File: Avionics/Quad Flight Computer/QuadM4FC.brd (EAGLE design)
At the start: 160 x 100 mm, 1 part, among them U1 INF-PG-LQFP-100-11-7000X7000E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

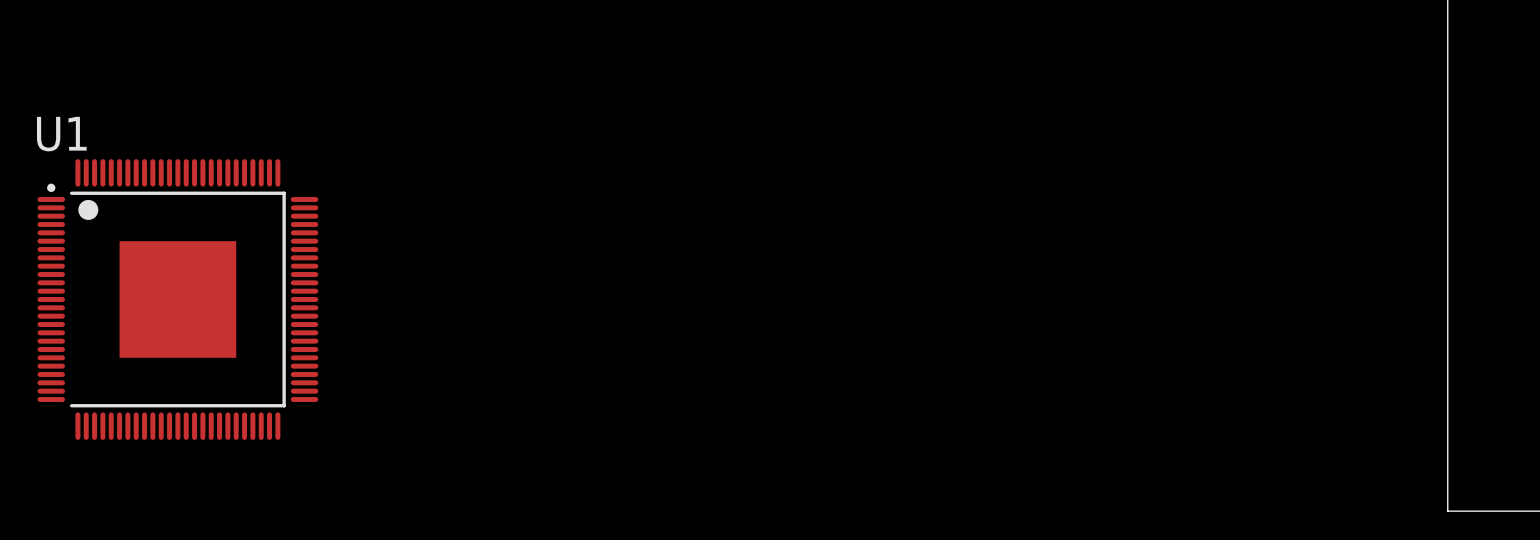
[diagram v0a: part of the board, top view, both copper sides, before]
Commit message: Added avionics library as Eagle-Library submodule.
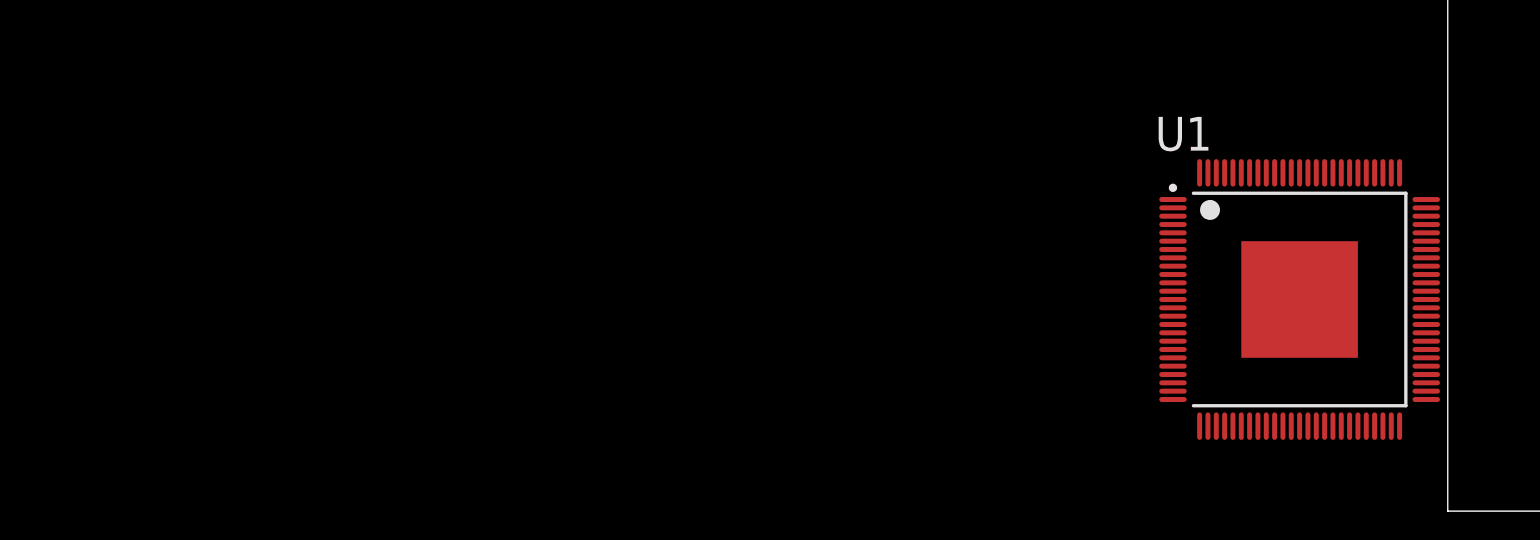
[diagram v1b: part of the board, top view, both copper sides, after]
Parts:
- moved U1 67.3 mm to (-8.89, 12.7)
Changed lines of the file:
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@@
 </autorouter>
 <elements>
-<element name="U1" library="XMC4500-F100K1024 AB" package="INF-PG-LQFP-100-11-7000X7000E9PRIMARY" value="INF-PG-LQFP-100-11-7000X7000E9LQFP-100" x="-76.2" y="12.7"/>
+<element name="U1" library="XMC4500-F100K1024 AB" package="INF-PG-LQFP-100-11-7000X7000E9PRIMARY" value="INF-PG-LQFP-100-11-7000X7000E9LQFP-100" x="-8.89" y="12.7"/>
 </elements>
 <signals>

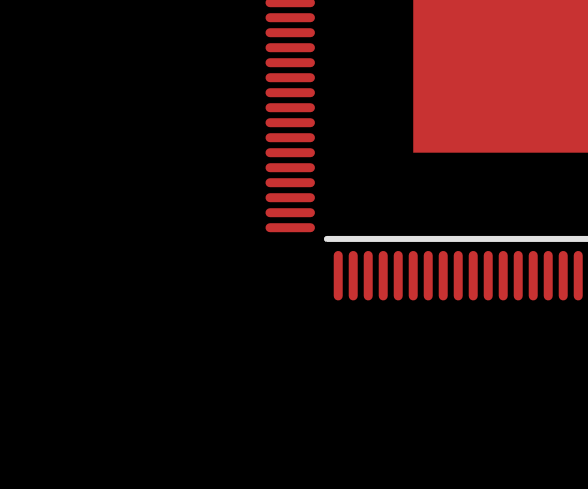
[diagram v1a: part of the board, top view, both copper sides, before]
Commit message: Added IMU to library
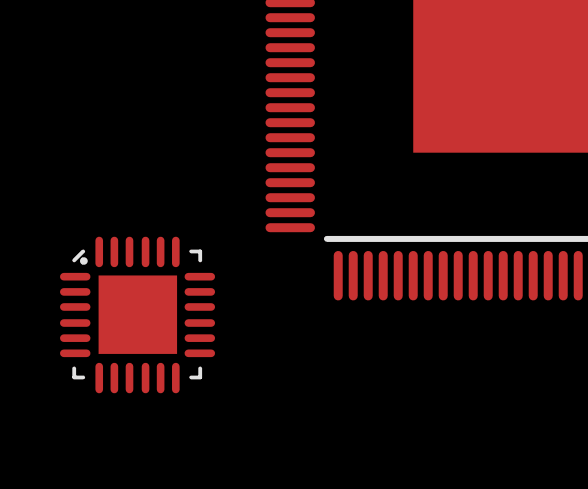
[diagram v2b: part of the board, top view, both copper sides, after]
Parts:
- added U2: MPU-9250, Invesense:QFN-24-4MM2
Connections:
- new net GND: U2.18, U2.P$1
- new net RESV_GND: U2.20
- new net RESV_VDDIO: U2.1
- new net VDD: U2.13
- new net VDDIO: U2.8
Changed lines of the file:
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@@
 <layer number="48" name="Document" color="7" fill="1" visible="yes" active="yes"/>
 <layer number="49" name="Reference" color="7" fill="1" visible="yes" active="yes"/>
+<layer number="50" name="dxf" color="7" fill="1" visible="yes" active="yes"/>
 <layer number="51" name="tDocu" color="7" fill="1" visible="yes" active="yes"/>
 <layer number="52" name="bDocu" color="7" fill="1" visible="yes" active="yes"/>
+<layer number="53" name="tGND_GNDA" color="7" fill="1" visible="yes" active="yes"/>
+<layer number="54" name="bGND_GNDA" color="7" fill="1" visible="yes" active="yes"/>
+<layer number="56" name="wert" color="7" fill="1" visible="yes" active="yes"/>
 <layer number="91" name="Nets" color="2" fill="1" visible="no" active="no"/>
 <layer number="92" name="Busses" color="1" fill="1" visible="no" active="no"/>
@@
 <layer number="97" name="Info" color="7" fill="1" visible="no" active="no"/>
 <layer number="98" name="Guide" color="6" fill="1" visible="no" active="no"/>
+<layer number="100" name="Muster" color="7" fill="1" visible="yes" active="yes"/>
+<layer number="101" name="Patch_Top" color="7" fill="1" visible="yes" active="yes"/>
+<layer number="102" name="Vscore" color="7" fill="1" visible="yes" active="yes"/>
+<layer number="103" name="tMap" color="7" fill="1" visible="yes" active="yes"/>
+<layer number="104" name="Name" color="7" fill="1" visible="yes" active="yes"/>
+<layer number="105" name="tPlate" color="7" fill="1" visible="yes" active="yes"/>
+<layer number="106" name="bPlate" color="7" fill="1" visible="yes" active="yes"/>
+<layer number="107" name="Crop" color="7" fill="1" visible="yes" active="yes"/>
+<layer number="108" name="fp8" color="7" fill="1" visible="yes" active="yes"/>
+<layer number="109" name="fp9" color="7" fill="1" visible="yes" active="yes"/>
+<layer number="110" name="fp0" color="7" fill="1" visible="yes" active="yes"/>
+<layer number="116" name="Patch_BOT" color="7" fill="1" visible="yes" active="yes"/>
+<layer number="121" name="_tsilk" color="7" fill="1" visible="yes" active="yes"/>
+<layer number="122" name="_bsilk" color="7" fill="1" visible="yes" active="yes"/>
+<layer number="123" name="tTestmark" color="7" fill="1" visible="yes" active="yes"/>
+<layer number="124" name="bTestmark" color="7" fill="1" visible="yes" active="yes"/>
+<layer number="125" name="_tNames" color="7" fill="1" visible="yes" active="yes"/>
+<layer number="131" name="tAdjust" color="7" fill="1" visible="yes" active="yes"/>
+<layer number="132" name="bAdjust" color="7" fill="1" visible="yes" active="yes"/>
+<layer number="144" name="Drill_legend" color="7" fill="1" visible="yes" active="yes"/>
+<layer number="151" name="HeatSink" color="7" fill="1" visible="yes" active="yes"/>
+<layer number="199" name="Contour" color="7" fill="1" visible="yes" active="yes"/>
+<layer number="200" name="200bmp" color="7" fill="1" visible="yes" active="yes"/>
+<layer number="201" name="201bmp" color="7" fill="1" visible="yes" active="yes"/>
+<layer number="202" name="202bmp" color="7" fill="1" visible="yes" active="yes"/>
+<layer number="203" name="203bmp" color="7" fill="1" visible="yes" active="yes"/>
+<layer number="204" name="204bmp" color="7" fill="1" visible="yes" active="yes"/>
+<layer number="205" name="205bmp" color="7" fill="1" visible="yes" active="yes"/>
+<layer number="206" name="206bmp" color="7" fill="1" visible="yes" active="yes"/>
+<layer number="207" name="207bmp" color="7" fill="1" visible="yes" active="yes"/>
+<layer number="208" name="208bmp" color="7" fill="1" visible="yes" active="yes"/>
+<layer number="209" name="209bmp" color="7" fill="1" visible="yes" active="yes"/>
+<layer number="210" name="210bmp" color="7" fill="1" visible="yes" active="yes"/>
+<layer number="211" name="211bmp" color="7" fill="1" visible="yes" active="yes"/>
+<layer number="212" name="212bmp" color="7" fill="1" visible="yes" active="yes"/>
+<layer number="213" name="213bmp" color="7" fill="1" visible="yes" active="yes"/>
+<layer number="214" name="214bmp" color="7" fill="1" visible="yes" active="yes"/>
+<layer number="215" name="215bmp" color="7" fill="1" visible="yes" active="yes"/>
+<layer number="216" name="216bmp" color="7" fill="1" visible="yes" active="yes"/>
+<layer number="217" name="217bmp" color="7" fill="1" visible="yes" active="yes"/>
+<layer number="218" name="218bmp" color="7" fill="1" visible="yes" active="yes"/>
+<layer number="219" name="219bmp" color="7" fill="1" visible="yes" active="yes"/>
+<layer number="220" name="220bmp" color="7" fill="1" visible="yes" active="yes"/>
+<layer number="221" name="221bmp" color="7" fill="1" visible="yes" active="yes"/>
+<layer number="222" name="222bmp" color="7" fill="1" visible="yes" active="yes"/>
+<layer number="223" name="223bmp" color="7" fill="1" visible="yes" active="yes"/>
+<layer number="224" name="224bmp" color="7" fill="1" visible="yes" active="yes"/>
+<layer number="250" name="Descript" color="7" fill="1" visible="yes" active="yes"/>
+<layer number="251" name="SMDround" color="7" fill="1" visible="yes" active="yes"/>
+<layer number="254" name="cooling" color="7" fill="1" visible="yes" active="yes"/>
 </layers>
 <board>
@@
 <elements>
 <element name="U1" library="XMC4500-F100K1024 AB" package="INF-PG-LQFP-100-11-7000X7000E9PRIMARY" value="INF-PG-LQFP-100-11-7000X7000E9LQFP-100" x="-8.89" y="12.7"/>
+<element name="U2" library="Invesense" package="QFN-24-4MM2" value="MPU-9250" x="-21.59" y="3.81"/>
 </elements>
 <signals>
+<signal name="GND">
+<contactref element="U2" pad="P$1"/>
+<contactref element="U2" pad="18"/>
+<wire x1="-19.5038" y1="5.0667" x2="-21.57" y2="3.8" width="0" layer="19" extent="1-1"/>
+</signal>
+<signal name="VDD">
+<contactref element="U2" pad="13"/>
+</signal>
+<signal name="RESV_GND">
+<contactref element="U2" pad="20"/>
+</signal>
+<signal name="VDDIO">
+<contactref element="U2" pad="8"/>
+</signal>
+<signal name="RESV_VDDIO">
+<contactref element="U2" pad="1"/>
+</signal>
 </signals>
 </board>

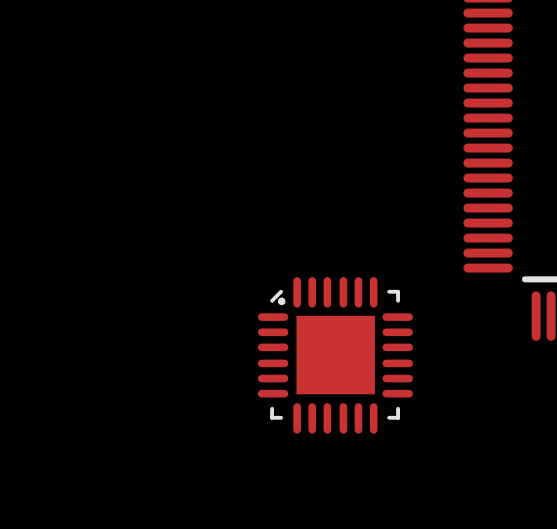
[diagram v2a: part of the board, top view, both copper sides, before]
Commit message: Added barometer
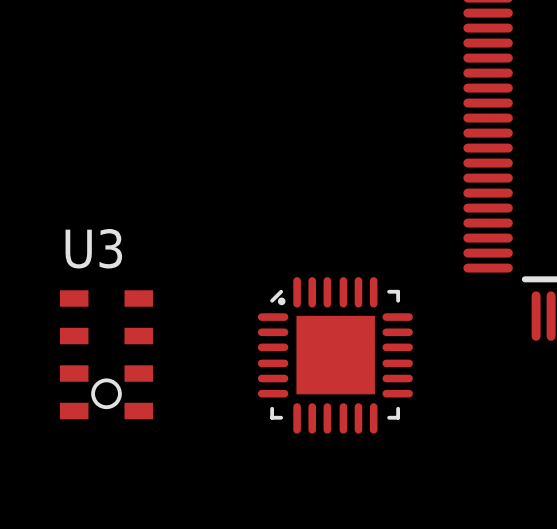
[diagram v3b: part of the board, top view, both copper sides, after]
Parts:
- added U3: MPL115A2, Sensors:MPL115A2
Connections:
- net GND: now also U2.EP; no longer U2.P$1
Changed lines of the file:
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@@
 <element name="U1" library="XMC4500-F100K1024 AB" package="INF-PG-LQFP-100-11-7000X7000E9PRIMARY" value="INF-PG-LQFP-100-11-7000X7000E9LQFP-100" x="-8.89" y="12.7"/>
 <element name="U2" library="Invesense" package="QFN-24-4MM2" value="MPU-9250" x="-21.59" y="3.81"/>
+<element name="U3" library="Sensors" package="MPL115A2" value="MPL115A2" x="-29.21" y="3.81"/>
 </elements>
 <signals>
 <signal name="GND">
-<contactref element="U2" pad="P$1"/>
 <contactref element="U2" pad="18"/>
+<contactref element="U2" pad="EP"/>
 <wire x1="-19.5038" y1="5.0667" x2="-21.57" y2="3.8" width="0" layer="19" extent="1-1"/>
 </signal>

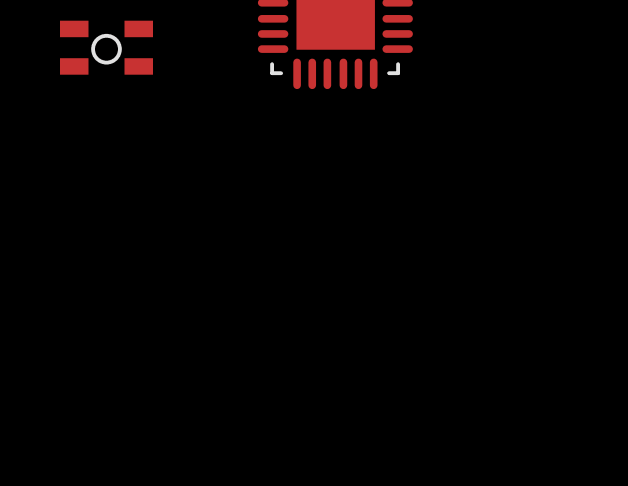
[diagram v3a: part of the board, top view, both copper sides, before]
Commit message: Added memory module
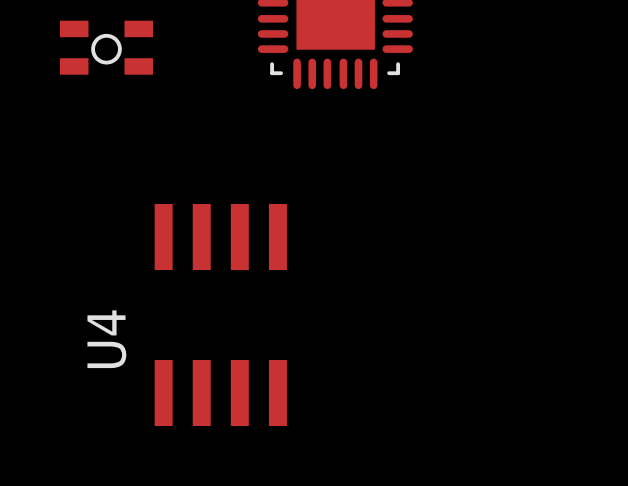
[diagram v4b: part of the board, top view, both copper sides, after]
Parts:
- added U4: S25FL127S, memory:SO8
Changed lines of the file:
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@@
 <element name="U2" library="Invesense" package="QFN-24-4MM2" value="MPU-9250" x="-21.59" y="3.81"/>
 <element name="U3" library="Sensors" package="MPL115A2" value="MPL115A2" x="-29.21" y="3.81"/>
+<element name="U4" library="memory" package="SO8" value="S25FL127S" x="-25.4" y="-6.35"/>
 </elements>
 <signals>

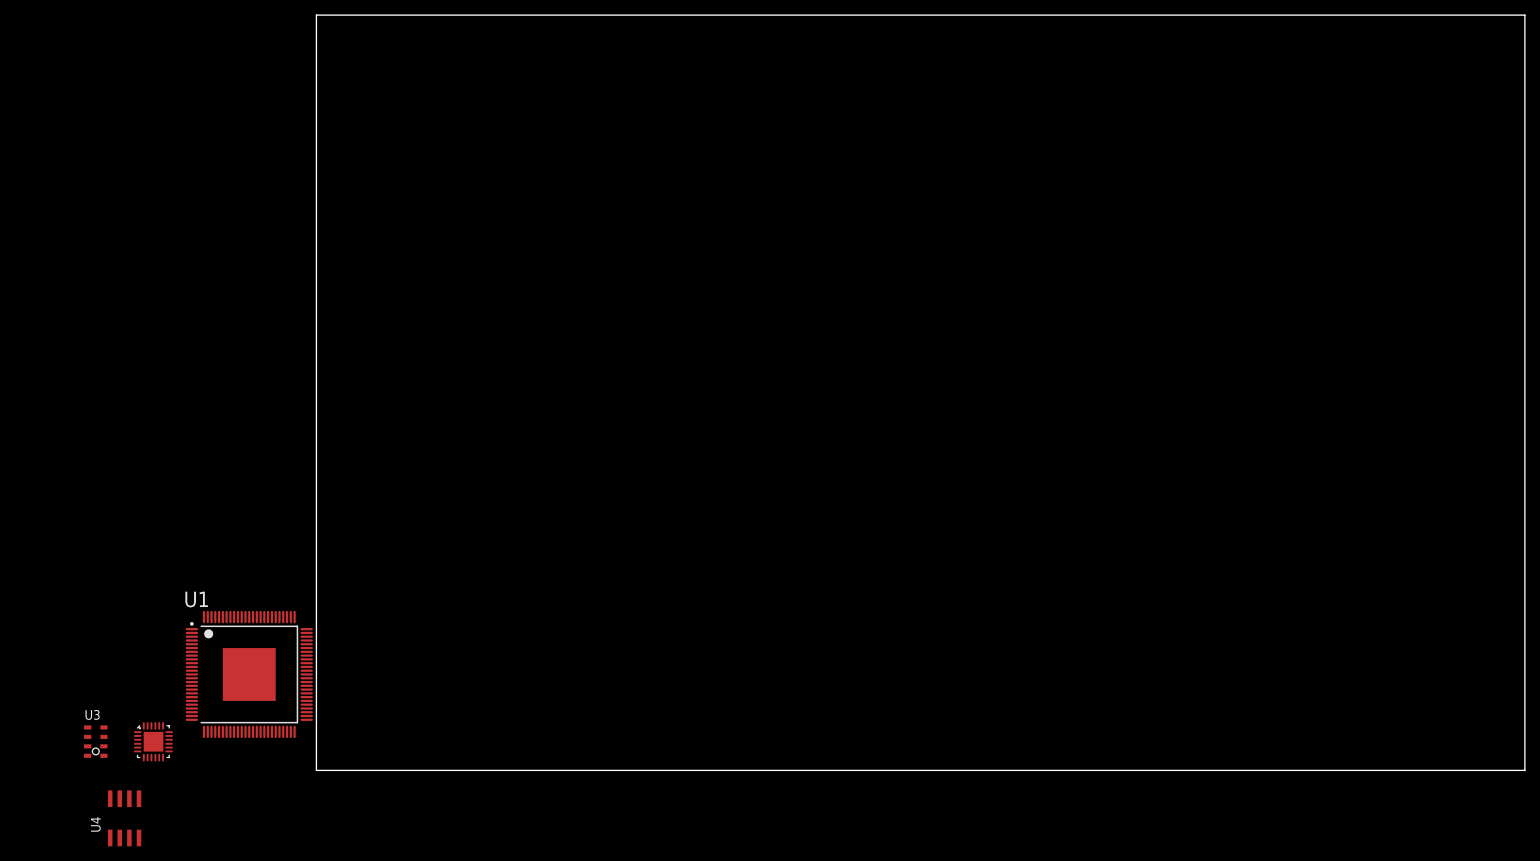
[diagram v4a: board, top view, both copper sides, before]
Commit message: Added radio part
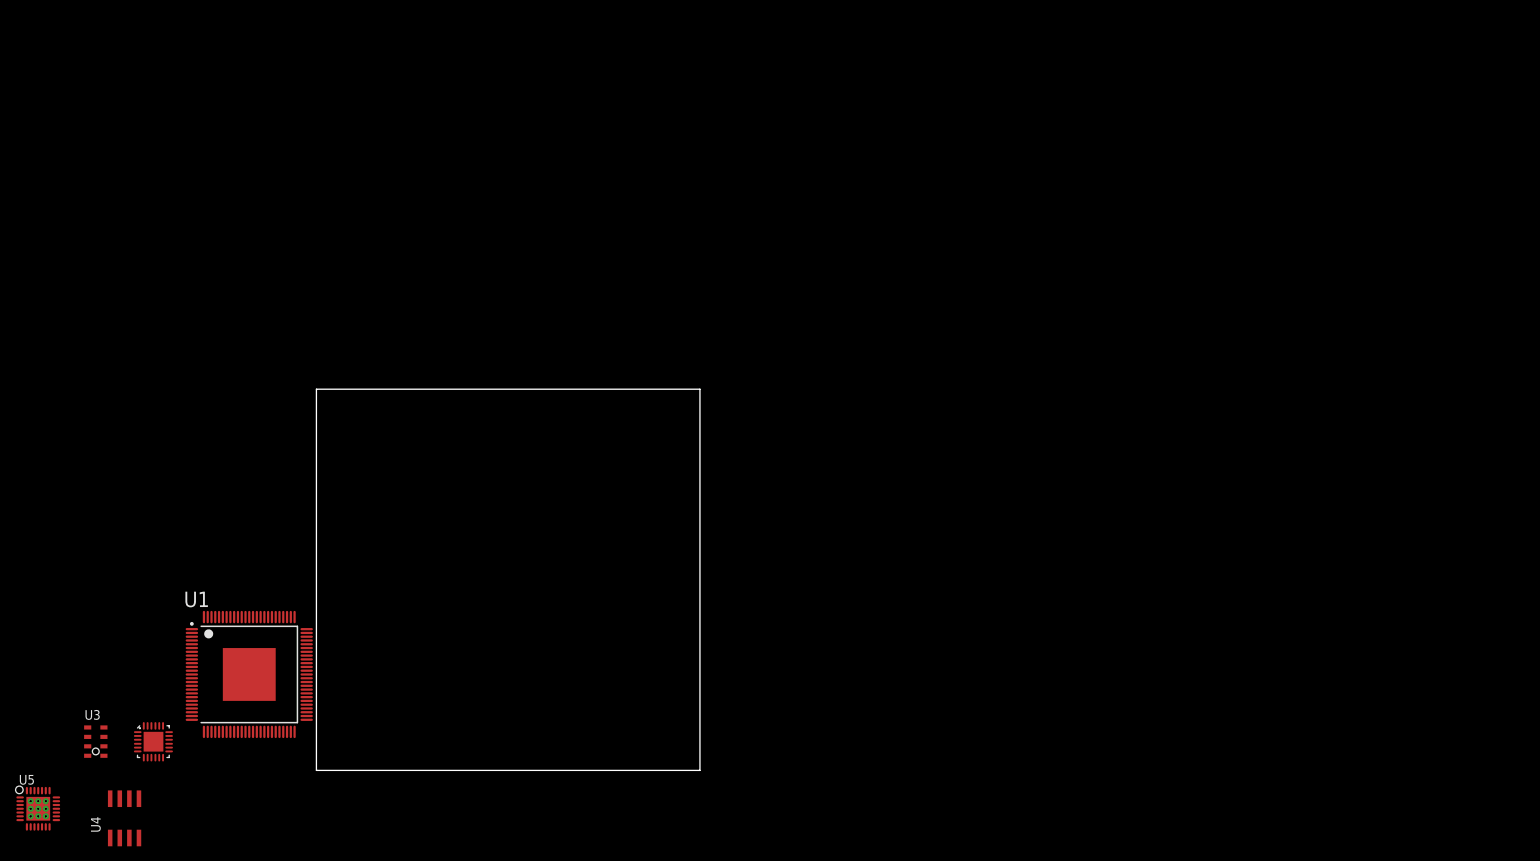
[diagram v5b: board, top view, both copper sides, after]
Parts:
- added U5: CC2520, ti_rf:RHD_S-PVQFN-N28
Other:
- board size 160 x 100 mm -> 50.8 x 50.5 mm
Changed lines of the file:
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@@
 <board>
 <plain>
-<wire x1="0" y1="0" x2="160" y2="0" width="0" layer="20"/>
-<wire x1="160" y1="0" x2="160" y2="100" width="0" layer="20"/>
-<wire x1="160" y1="100" x2="0" y2="100" width="0" layer="20"/>
-<wire x1="0" y1="100" x2="0" y2="0" width="0" layer="20"/>
+<wire x1="0" y1="0" x2="50.78" y2="0" width="0" layer="20"/>
+<wire x1="50.78" y1="0" x2="50.78" y2="50.47" width="0" layer="20"/>
+<wire x1="50.78" y1="50.47" x2="0" y2="50.47" width="0" layer="20"/>
+<wire x1="0" y1="50.47" x2="0" y2="0" width="0" layer="20"/>
 </plain>
 <attributes>
@@
 <element name="U3" library="Sensors" package="MPL115A2" value="MPL115A2" x="-29.21" y="3.81"/>
 <element name="U4" library="memory" package="SO8" value="S25FL127S" x="-25.4" y="-6.35"/>
+<element name="U5" library="ti_rf" package="RHD_S-PVQFN-N28" value="CC2520" x="-36.83" y="-5.08"/>
 </elements>
 <signals>
